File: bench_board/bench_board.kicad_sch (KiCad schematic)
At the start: 42 parts, among them J1 BATT_2S, J2 BOOT0_JUMPER, J3 USB-C, J4 CRSF_UART, J5 DSHOT_M1-M4, J6 SWD, U1 STM32F405RGT6, U2 TPS563201, U3 AMS1117-3.3, U4 MPU-6000, U5 USBLC6-2SC6, Y1 8MHz

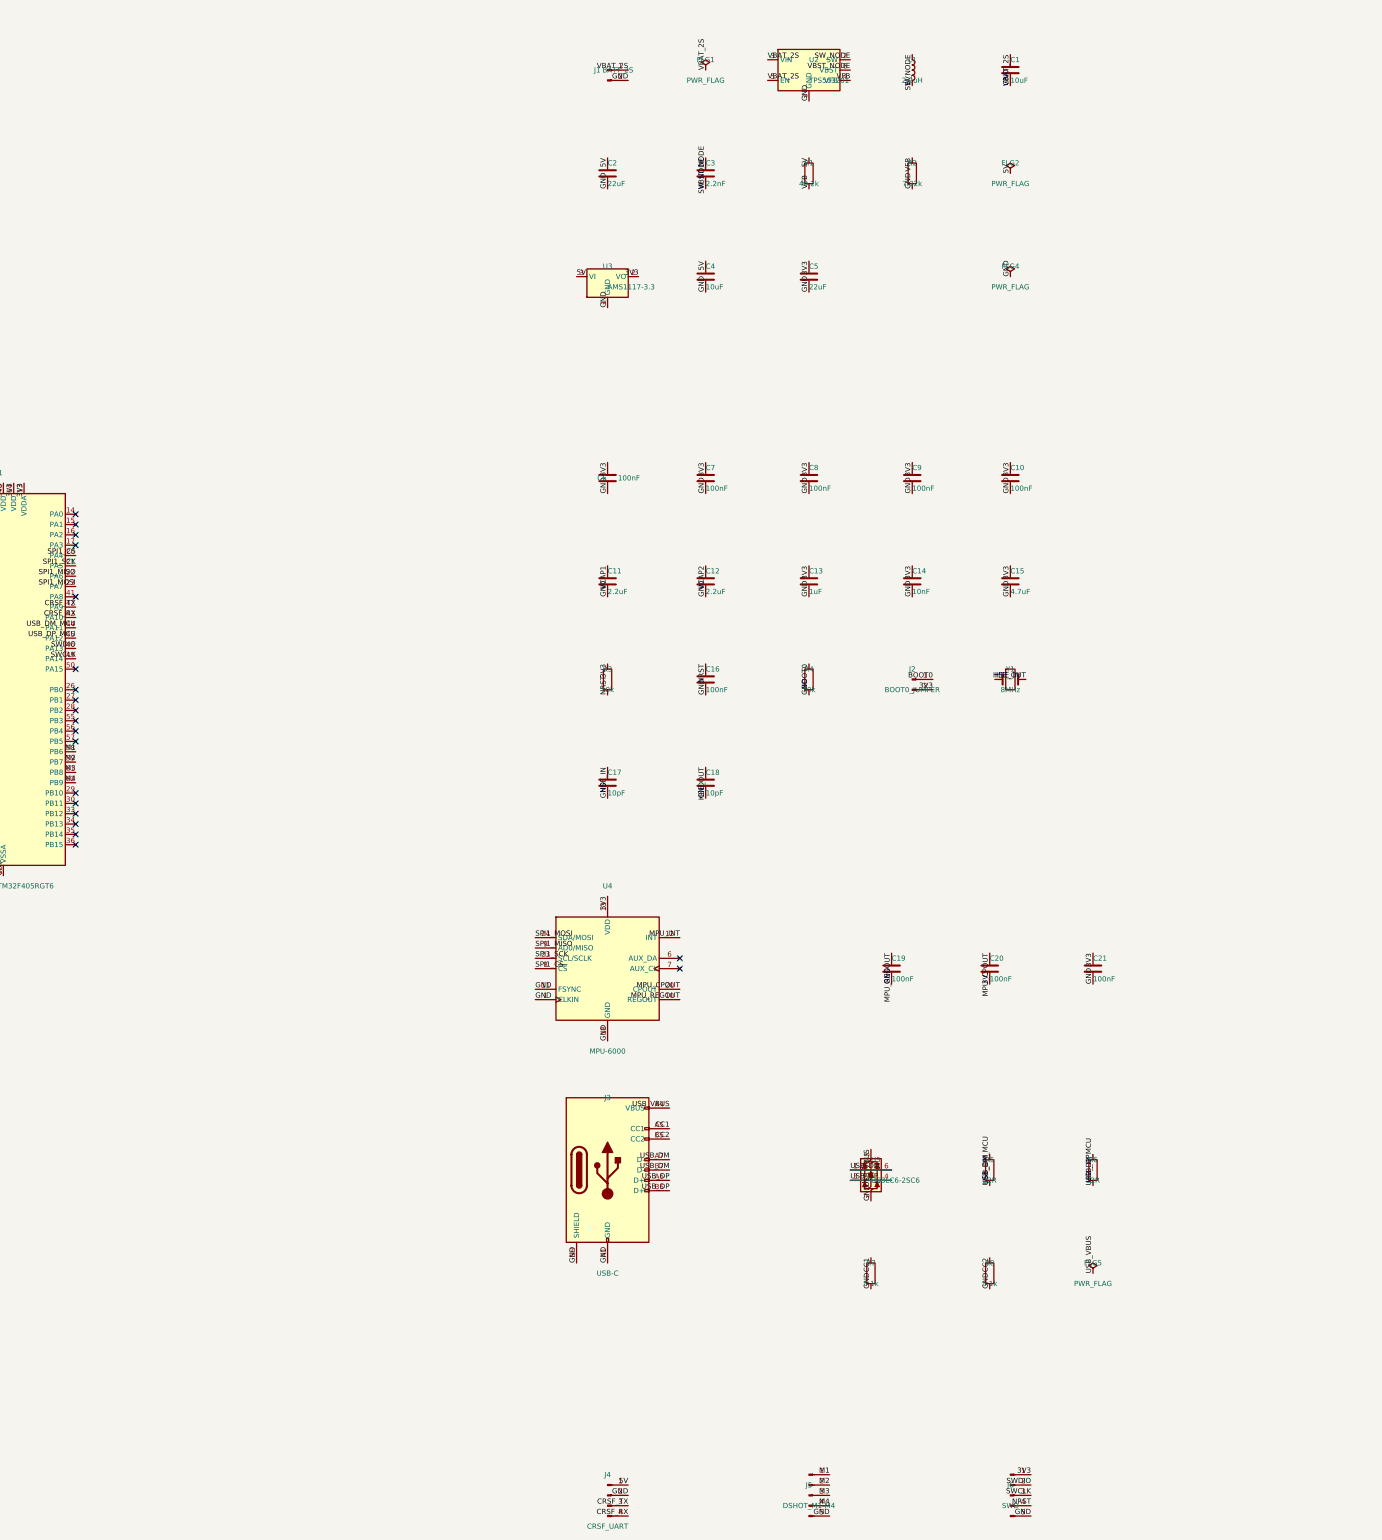
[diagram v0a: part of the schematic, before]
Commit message: Rework power tree to single-stage buck (3.3V direct); add battery-sense divider
Deletes the AMS1117 5V->3.3V LDO stage and its caps -- the 2-stage
buck-then-LDO topology forced the buck to hold 5V from a 2S pack whose
6.0V floor leaves only 1V of headroom (~83% duty cycle, at/past most buck
ICs' practical limit). TPS563201 now regulates directly to 3.3V (feedback
divider R1/R2 retargeted: 33.2k/10.0k, Vref=0.768V -> ~3.30V), which is
what every load on this board (STM32F405, MPU-6000, DShot signal levels)
actually wants. Duty cycle at 6.0V floor is now ~55%; at 8.4V ceiling
~39% -- comfortable across the whole battery range, both ends far from the
TPS563201's ~90% max-duty limit.

Inductor re-sized for the new operating point: L1 2.2uH -> 10uH, sized for
~23% ripple current at a 1.5A load estimate (worst-case ripple is at
Vin=8.4V, the max input, not the 6.0V floor). C2 (22uF output cap,
unchanged) gives ~7mV ripple at that current, comfortable margin. Thermal
margin is now single-stage only (~0.5W in the buck at 1.5A/90% eff, ~33C
rise in a SOT-23-6 package) instead of also carrying the LDO's dropout
heat, which was the dominant loss term in the old topology.

Also fixed a real latent bug found while touching this circuit: C3, the
TPS563201's SW-to-BOOST bootstrap cap, was 2.2nF -- roughly two orders of
magnitude under the ~100nF a D-CAP2/D-CAP3 synchronous buck needs to hold
the high-side gate charge, especially at the now-much-lower duty cycles.
Corrected to 100nF.

CRSF_UART's receiver-power pin (J4/1) now carries 3V3 instead of the
deleted 5V rail. Per the Build Plan: the many 5V-only ELRS nano receivers
this affects get resolved by picking a 3.3V-capable receiver in Stage 2
part selection, not by adding a rail back.

Battery-sense divider added (genuine prior omission -- no low-voltage
cutoff existed anywhere): R9 (20.0k, VBAT_2S side) / R10 (10.0k, GND
side), 1% resistors, into PA0 (ADC123_IN0, previously unused) with a
100nF filter cap (C22). Divide-by-3.0 r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
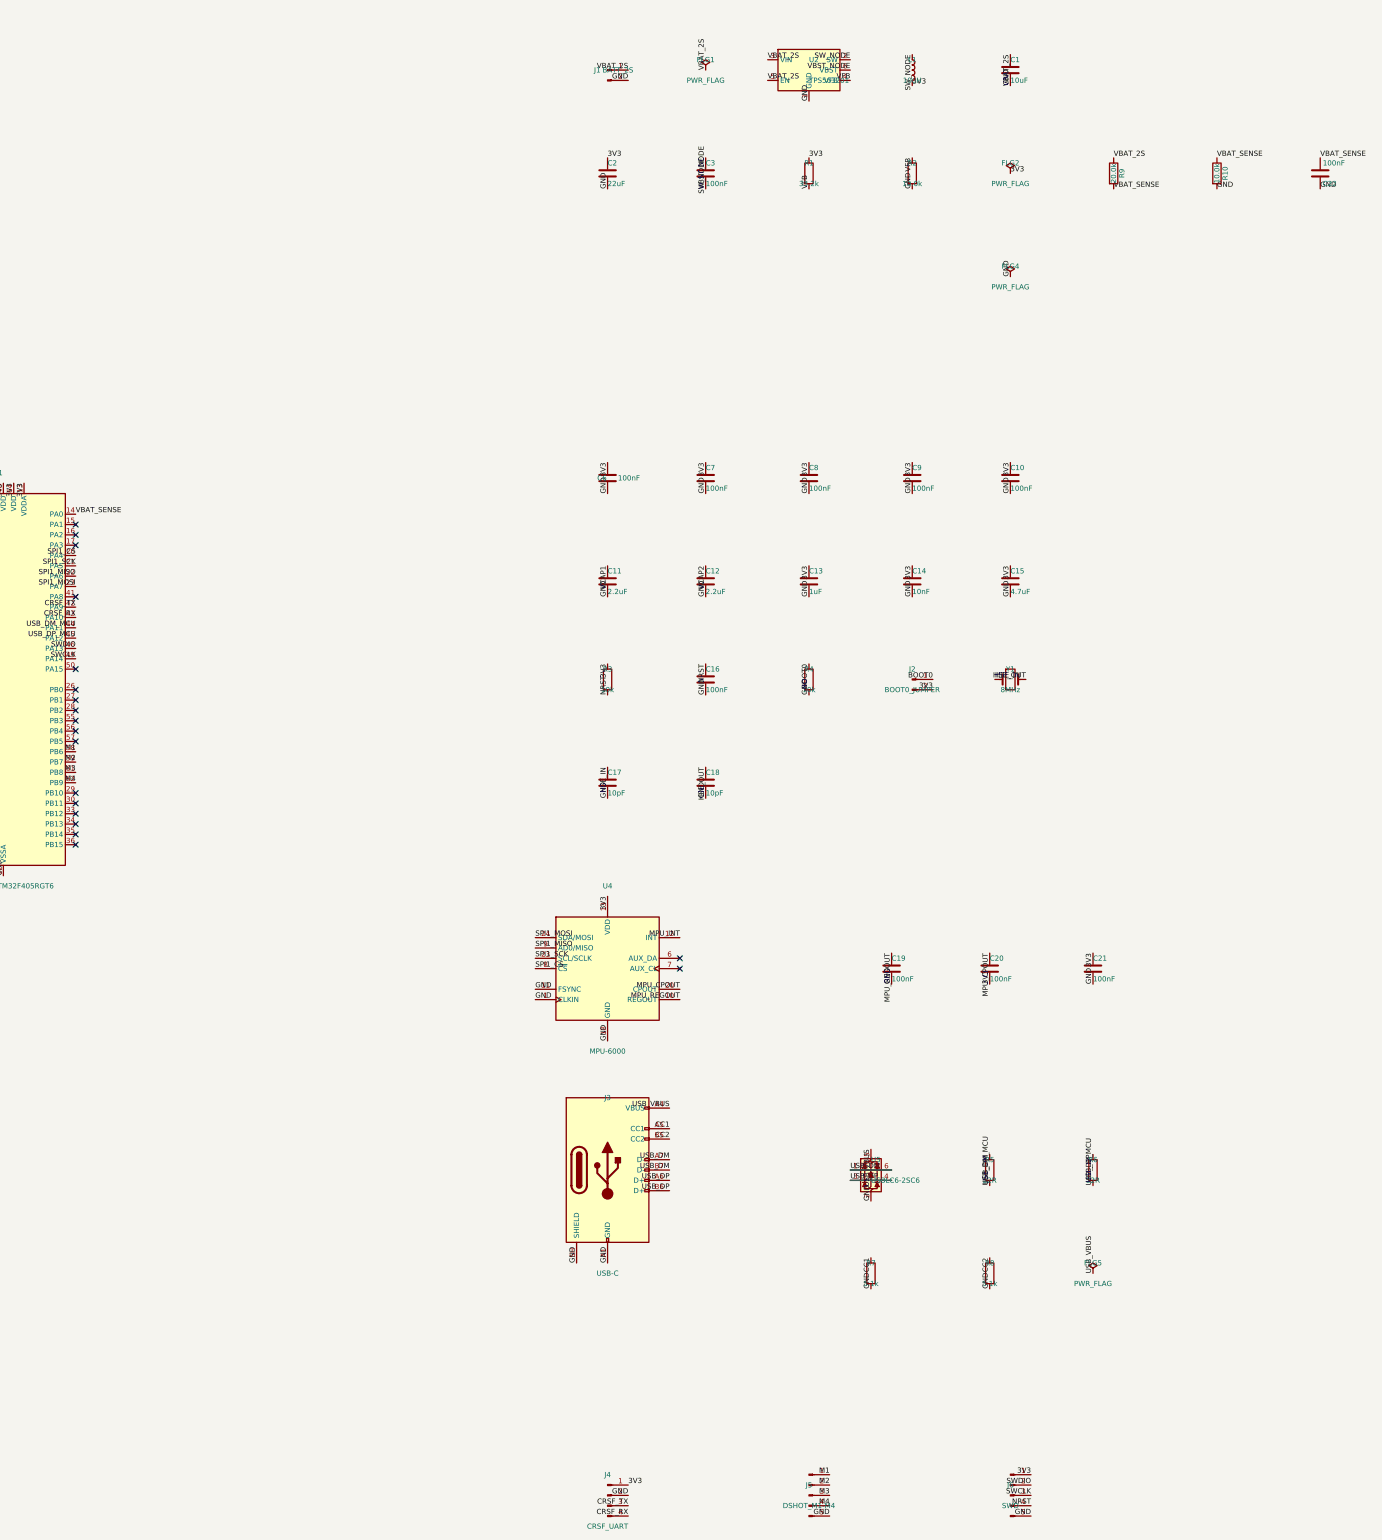
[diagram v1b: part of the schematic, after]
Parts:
- removed C4: 10uF, Capacitor_SMD:C_0805_2012Metric, symbol Device:C
- removed C5: 22uF, Capacitor_SMD:C_0805_2012Metric, symbol Device:C
- removed U3: AMS1117-3.3, Package_TO_SOT_SMD:SOT-223-3_TabPin2, symbol Regulator_Linear:AMS1117-3.3
- added C22: 100nF, Capacitor_SMD:C_0402_1005Metric, symbol Device:C
- added R10: 10.0k, Resistor_SMD:R_0402_1005Metric, symbol Device:R
- added R9: 20.0k, Resistor_SMD:R_0402_1005Metric, symbol Device:R
- C3: value 2.2nF -> 100nF
- L1: value 2.2uH -> 10uH
- R1: value 40.2k -> 33.2k
- R2: value 7.32k -> 10.0k
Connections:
- net 5V is gone; now on net 3V3: C2.1, J4.1 (Pin_1), L1.2, R1.1
- net GND: now also C22.2, R10.2
- net VBAT_2S: now also R9.1
- net VBAT_SENSE: now reaches U1.14 (PA0)
- net VBAT_SENSE: now also C22.1, R10.1, R9.2
- no-connect marks 36 -> 35
